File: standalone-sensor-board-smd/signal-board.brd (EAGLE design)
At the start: 26 x 93.5 mm, 32 parts, among them Q1 QRE1113, Q2 QRE1113, Q3 QRE1113, Q4 QRE1113, Q5 QRE1113, Q6 QRE1113, Q7 QRE1113, U1 CD4051BE

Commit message: add smd boards from standalone
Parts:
- removed D1, D2, D3, D4, D5, D6, D7: 1655, 1655:LED_1655
- removed FFCIN, FFCOUT: 52806-1410, 52806-1410:528061410
- removed Q1, Q2, Q3, Q4, Q5, Q6, Q7: QRE1113, qre1113:DIP4_100AQ_ONS
- removed R1, R11, R13, R3, R5, R7, R9: 100, rcl:0207/10
- removed RDV: 100k, rcl:0207/10
- added J1: sensors, 686114148922:686114148922
- added J3: to_next_board, 686114148922:686114148922
- added J4: to_controller, 686114148922:686114148922
- added LED1, LED2, LED3, LED4, LED5, LED6, LED7: WS2812B3535, adafruit:LED3535
- added RDV1, RDV2, RDV3, RDV4, RDV5, RDV6, RDV7: 100k, rcl:0207/10
- moved U1 53.3 mm to (19.4, 38.9), turned to 180 degrees
- moved SJ7 19.4 mm to (3.00, 80.0), flipped to the top, turned to 270 degrees
- moved SJ6 16.6 mm to (5.00, 80.0), flipped to the top, turned to 270 degrees
- moved SJ5 13.9 mm to (7.00, 80.0), flipped to the top, turned to 270 degrees
- moved SJ4 11.2 mm to (9.00, 80.0), flipped to the top, turned to 270 degrees
- moved SJ3 8.54 mm to (11.0, 80.0), flipped to the top, turned to 270 degrees
- moved SJ2 6.08 mm to (13.0, 80.0), flipped to the top, turned to 270 degrees
- moved SJ1 4.12 mm to (15.0, 80.0), flipped to the top, turned to 270 degrees
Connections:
- removed net N$11: Q6.1, R11.2
- removed net N$13: Q7.1, R13.2
- removed net N$15: D6.4, D7.2
- removed net N$16: D1.4, D2.2
- removed net N$17: D2.4, D3.2
- removed net N$18: D3.4, D4.2
- removed net N$19: D4.4, D5.2
- removed net N$20: D5.4, D6.2
- removed net N$7: Q4.1, R7.2
- new net N$4: LED4.3, LED5.1
- new net N$6: LED6.3, LED7.1
- net 3V: now also J3.2, J4.13, LED1.2, LED2.2, LED3.2, LED4.2, LED5.2, LED6.2, LED7.2; no longer D1.3, D2.3, D3.3, D4.3, D5.3, D6.3, D7.3, FFCIN.13, FFCOUT.2
- net A: now also J3.4, J4.11; no longer FFCIN.11, FFCOUT.4
- net B: now also J3.5, J4.10; no longer FFCIN.10, FFCOUT.5
- net C: now also J3.6, J4.9; no longer FFCIN.9, FFCOUT.6
- net C0: now also J1.1, RDV1.2; no longer Q1.3
- net C1: now also J1.2, RDV2.2; no longer Q2.3
- net C2: now also J1.3, RDV3.2; no longer Q3.3
- net C3: now also J1.9, RDV4.2; no longer Q4.3
- net C4: now also J1.10, RDV5.2; no longer Q5.3
- net C5: now also J1.11, RDV6.2; no longer Q6.3
- net C6: now also J1.12, RDV7.2; no longer Q7.3
- net DIN: now also J4.8, LED1.1; no longer D1.2, FFCIN.8
- net DOUT: now also J3.7, LED7.3; no longer D7.4, FFCOUT.7
- net GND: now also J1.14, J1.MP1, J1.MP2, J3.1, J3.MP1, J3.MP2, J4.14, J4.MP1, J4.MP2, LED1.4, LED2.4, LED3.4, LED4.4, LED5.4, LED6.4, LED7.4; no longer D1.1, D2.1, D3.1, D4.1, D5.1, D6.1, D7.1, FFCOUT.1, Q1.2, Q1.4, Q2.2, Q2.4, Q3.2, Q3.4, Q4.2, Q4.4, Q5.2, Q5.4, Q6.2, Q6.4, Q7.2, Q7.4
- net N$1: now also LED1.3, LED2.1; no longer Q1.1, R1.2
- net N$2: now also LED2.3, LED3.1; no longer FFCOUT.3, R1.1, R11.1, R13.1, R3.1, R5.1, R7.1, R9.1
- net N$3: now also LED3.3, LED4.1; no longer Q2.1, R3.2
- net N$5: now also LED5.3, LED6.1; no longer Q3.1, R5.2
- net S1: now also J3.8, J4.7; no longer FFCIN.7, FFCOUT.8
- net S2: now also J3.9, J4.6; no longer FFCIN.6, FFCOUT.9
- net S3: now also J3.10, J4.5; no longer FFCIN.5, FFCOUT.10
- net S4: now also J3.11, J4.4; no longer FFCIN.4, FFCOUT.11
- net S5: now also J3.12, J4.3; no longer FFCIN.3, FFCOUT.12
- net S6: now also J3.13, J4.2; no longer FFCIN.2, FFCOUT.13
- net S7: now also J3.14, J4.1; no longer FFCIN.1, FFCOUT.14
- net SIG: no longer RDV.1
- net VCC: now also J1.13, J3.3, J4.12, RDV1.1, RDV2.1, RDV3.1, RDV4.1, RDV5.1, RDV6.1, RDV7.1; no longer FFCIN.12, RDV.2
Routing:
- net VCC: track 38.2 -> 169.6 mm, vias 0 -> 2
- net GND: track 108.9 -> 0.00 mm, vias 7 -> 0
- net N$13: track 60.4 -> 0.00 mm
- net N$11: track 49.1 -> 0.00 mm
- net 3V: track 122.7 -> 160.9 mm, vias 0 -> 9
- net C1: track 66.8 -> 30.4 mm, vias 3 -> 0
- net C0: track 50.8 -> 24.2 mm
- net N$7: track 25.3 -> 0.00 mm
- net A: track 65.9 -> 91.2 mm, vias 0 -> 2
- net C3: track 11.8 -> 35.8 mm, vias 2 -> 0
- net C: track 68.1 -> 90.7 mm, vias 0 -> 2
- net C2: track 15.8 -> 35.3 mm, vias 2 -> 0
- net C5: track 29.0 -> 47.2 mm
- net SIG: track 36.0 -> 51.9 mm
- net C4: track 18.1 -> 30.3 mm
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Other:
- board text added: "NEMUS Signal Board v0.1.0"
- board text removed: "NEMUS Face Board v0.1.1"

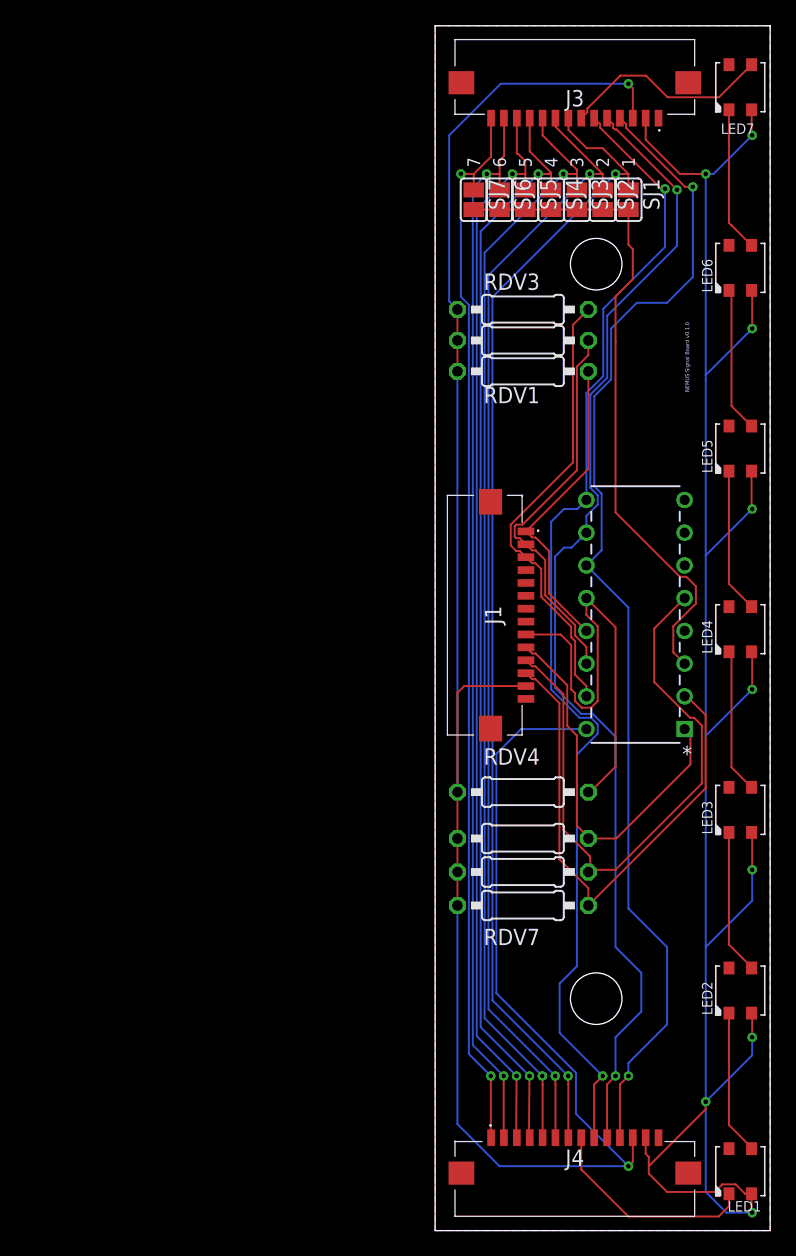
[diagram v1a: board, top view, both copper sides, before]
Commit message: add mounting holes
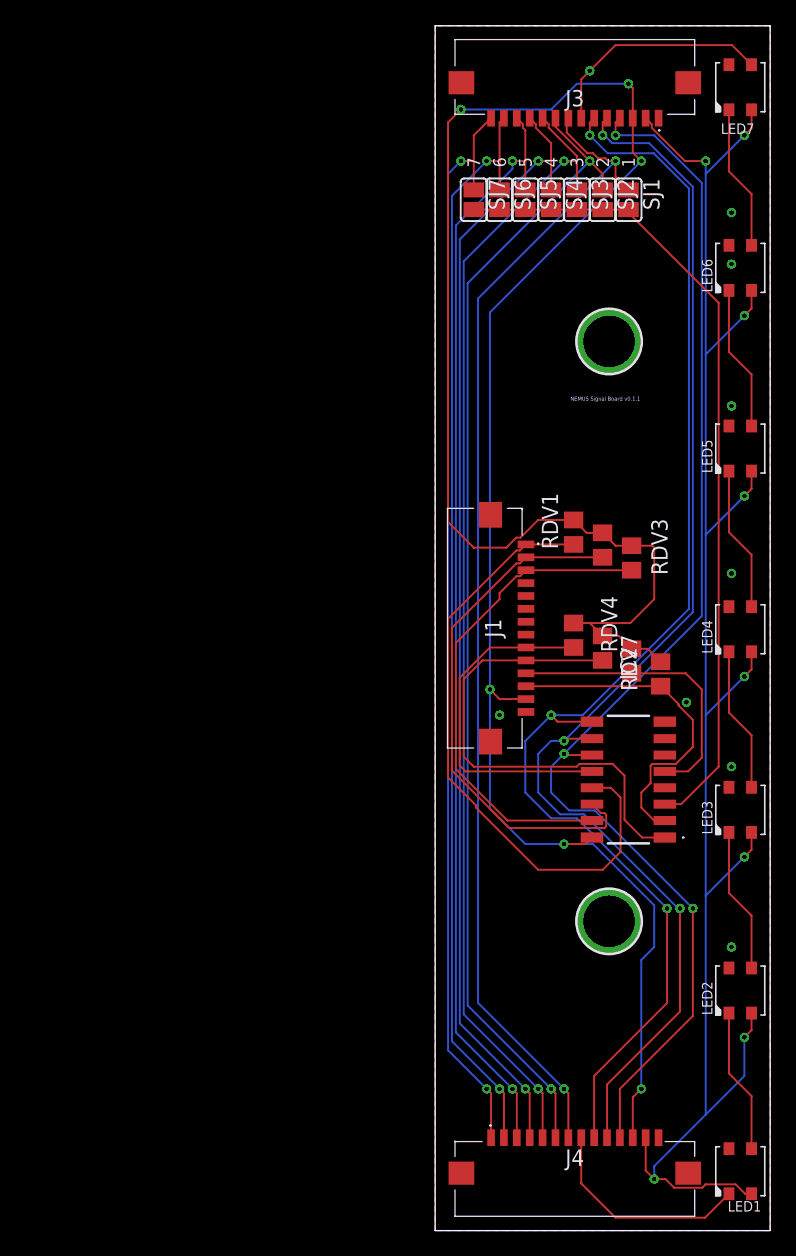
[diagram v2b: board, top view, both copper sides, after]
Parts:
- removed U1: CD4051BE, CD4051BE:N16
- added IC2: HEF4051BT,653, HEF4051BT_653:HEF4051BT653
- added U$1, U$2: MICROBUILDER_MOUNTINGHOLEMICROBUILDER_MOUNTINGHOL_4.0, microbuilder:MICROBUILDER_MOUNTINGHOLE_4.0_PLATEDTHIN
- RDV1, RDV2, RDV3, RDV4, RDV5, RDV6, RDV7: device rcl:0207/10 -> rcl:R0805
- moved RDV3 21.0 mm to (15.2, 52.2), turned to 270 degrees
- moved RDV7 20.9 mm to (17.5, 43.2), turned to 270 degrees
- moved RDV6 18.4 mm to (15.2, 44.2), turned to 270 degrees
- moved RDV2 17.0 mm to (13.0, 53.2), turned to 270 degrees
- moved RDV5 16.0 mm to (13.0, 45.2), turned to 270 degrees
- moved RDV1 13.1 mm to (10.8, 54.2), turned to 270 degrees
- moved RDV4 12.8 mm to (10.8, 46.2), turned to 270 degrees
- moved J1 1.01 mm to (4.00, 46.8)
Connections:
- net A: now also IC2.11; no longer U1.11
- net B: now also IC2.10; no longer U1.10
- net C: now also IC2.9; no longer U1.9
- net C0: now also IC2.13; no longer U1.13
- net C1: now also IC2.14; no longer U1.14
- net C2: now also IC2.15; no longer U1.15
- net C3: now also IC2.12; no longer U1.12
- net C4: now also IC2.1; no longer U1.1
- net C5: now also IC2.5; no longer U1.5
- net C6: now also IC2.2; no longer U1.2
- net GND: now also IC2.6, IC2.7, IC2.8; no longer U1.6, U1.7, U1.8
- net SIG: now also IC2.3; no longer U1.3
- net VCC: now also IC2.16; no longer U1.16
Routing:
- net C5: track 47.2 -> 22.8 mm
- net C0: track 24.2 -> 48.2 mm
- net 3V: track 160.9 -> 140.0 mm, vias 9 -> 8
- net VCC: track 169.6 -> 185.5 mm, vias 2 -> 6
- net C6: track 41.0 -> 25.9 mm
- net C: track 90.7 -> 102.7 mm, vias 2 -> 3
- net SIG: track 51.9 -> 63.5 mm
- net C1: track 30.4 -> 41.3 mm
- net B: track 90.6 -> 99.8 mm, vias 2 -> 3
- net C3: track 35.8 -> 27.1 mm
- net A: track 91.2 -> 98.9 mm, vias 2 -> 3
- net C4: track 30.3 -> 37.8 mm
- net C2: track 35.3 -> 38.3 mm
- net S6: track 83.0 -> 85.3 mm
- net S3: track 86.9 -> 89.2 mm
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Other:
- board text added: "NEMUS Signal Board v0.1.1"
- board text removed: "NEMUS Signal Board v0.1.0"
